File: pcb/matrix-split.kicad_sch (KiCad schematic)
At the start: 115 parts, among them J1 AudioJack4, J4 DBG, SW1 Switch, SW10 Switch, SW11 Switch, SW12 Switch, SW13 Switch, SW14 Switch, SW15 Switch, SW16 Switch, SW17 Switch, SW18 Switch, SW19 Switch, SW2 Switch, SW20 Switch, SW21 Switch, SW22 Switch, SW23 Switch, SW24 Switch, SW25 Switch, SW26 Switch, SW27 Switch, SW28 Switch, SW29 Switch, SW3 Switch, SW30 Reset_Switch, SW31 BootSel_Switch, SW4 Switch, SW5 Switch, SW6 Switch, SW7 Switch, SW8 Switch, SW9 Switch, U1 W25Q128JVS, U2 RP2040, U3 NCP1117-3.3_SOT223, Y1 Crystal_GND24

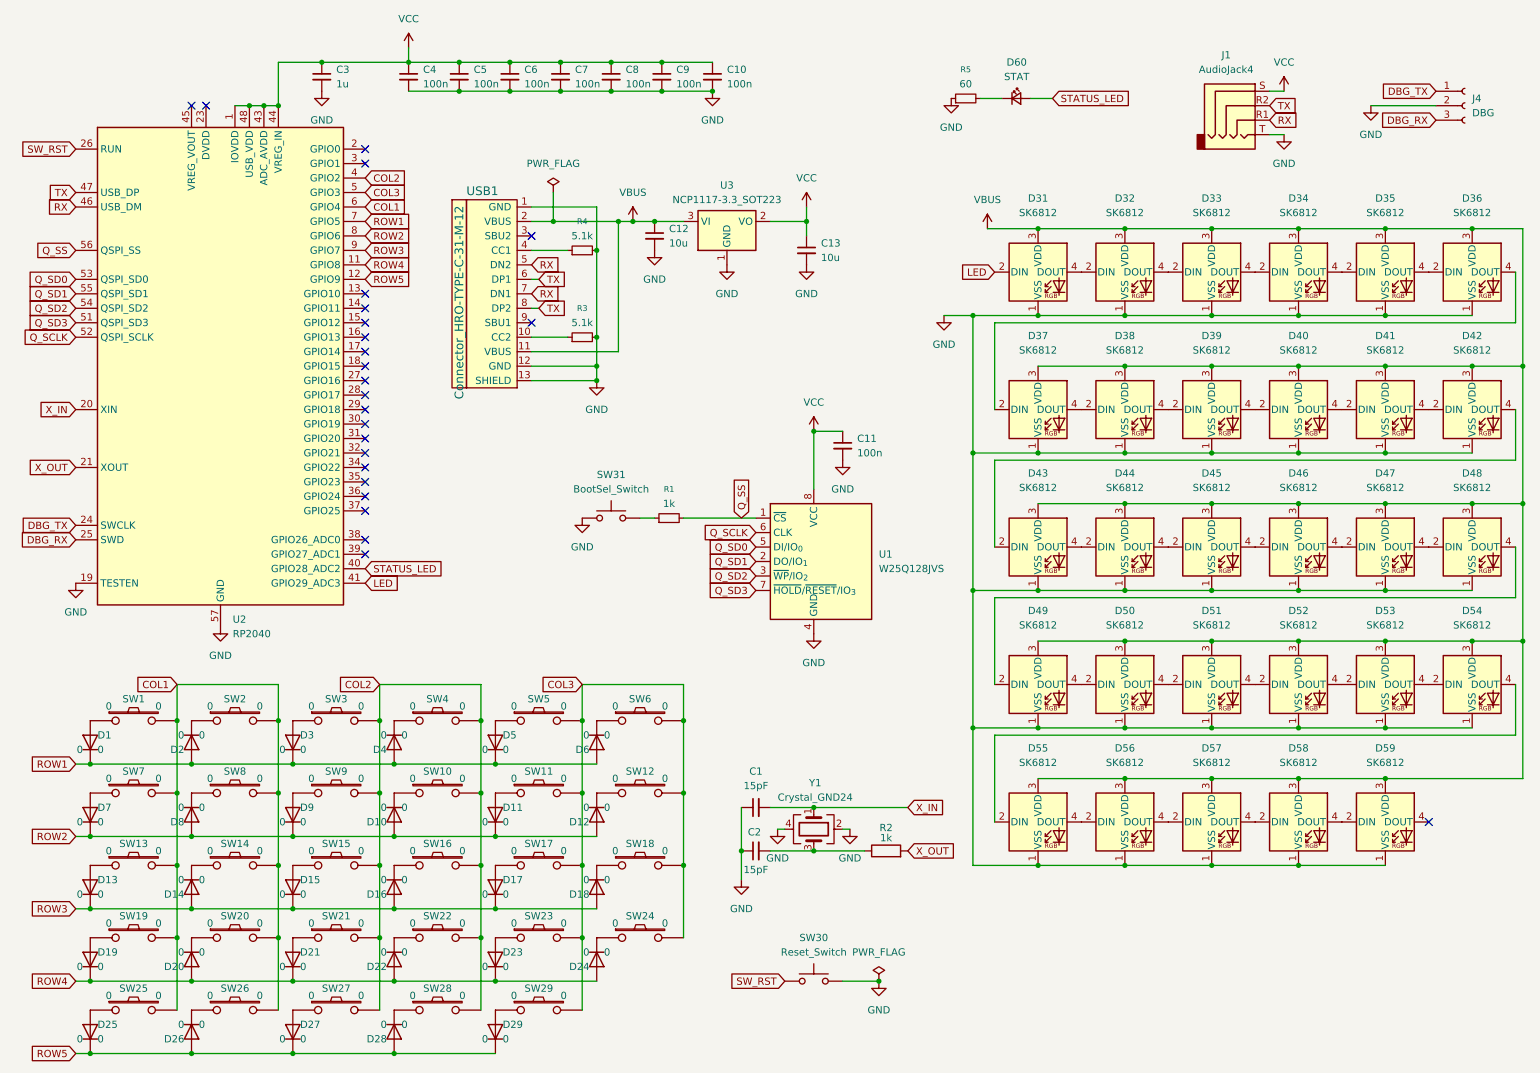
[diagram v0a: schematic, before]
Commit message: updating routing and pcb layout
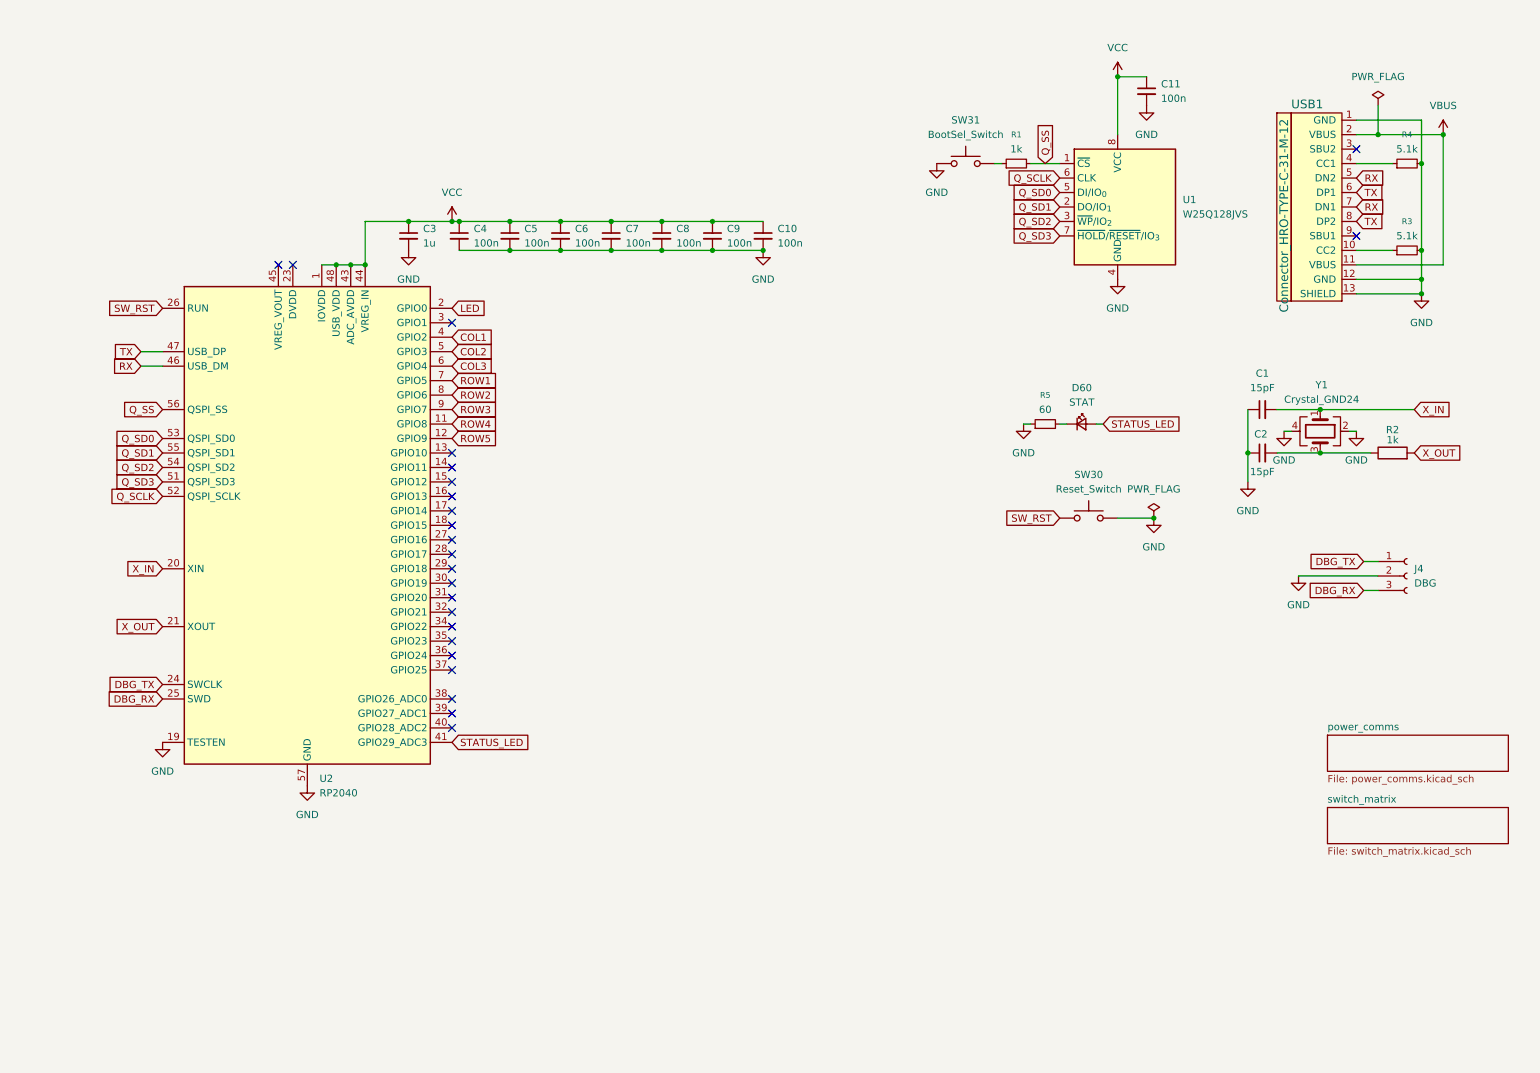
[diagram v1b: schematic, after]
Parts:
- removed C12, C13: 10u, Capacitor_SMD:C_0805_2012Metric, symbol Device:C_Small
- removed D1, D10, D11, D12, D13, D14, D15, D16, D17, D18, D19, D2, D20, D21, D22, D23, D24, D25, D26, D27, D28, D29, D3, D4, D5, D6, D7, D8, D9: Diode, Diode_SMD:D_0805_2012Metric, symbol zzkeeb:Diode
- removed D31, D32, D33, D34, D35, D36, D37, D38, D39, D40, D41, D42, D43, D44, D45, D46, D47, D48, D49, D50, D51, D52, D53, D54, D55, D56, D57, D58, D59: SK6812, LED_SMD:LED_SK6812_PLCC4_5.0x5.0mm_P3.2mm, symbol LED:SK6812
- removed J1: AudioJack4, PCM_marbastlib-xp-various:CON_MJ-4PP-9_Reversible, symbol Connector_Audio:AudioJack4
- removed SW1, SW10, SW11, SW12, SW13, SW14, SW15, SW16, SW17, SW18, SW19, SW2, SW20, SW21, SW22, SW23, SW24, SW25, SW26, SW27, SW28, SW29, SW3, SW4, SW5, SW6, SW7, SW8, SW9: Switch, keyswitches.pretty-master:Kailh_socket_PG1350, symbol zzkeeb:Switch
- removed U3: NCP1117-3.3_SOT223, Package_TO_SOT_SMD:SOT-223-3_TabPin2, symbol Regulator_Linear:NCP1117-3.3_SOT223
- USB1: footprint Type-C.pretty-master:HRO-TYPE-C-31-M-12-HandSoldering -> Type-C:HRO-TYPE-C-31-M-12-HandSoldering
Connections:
- net COL1: now also U2.4 (GPIO2); no longer U2.6 (GPIO4)
- net COL2: now also U2.5 (GPIO3); no longer U2.4 (GPIO2)
- net COL3: now also U2.6 (GPIO4); no longer U2.5 (GPIO3)
- net LED: now also U2.2 (GPIO0); no longer U2.41 (GPIO29_ADC3)
- net STATUS_LED: now also U2.41 (GPIO29_ADC3); no longer U2.40 (GPIO28_ADC2)
- no-connect marks 25 -> 24
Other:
- added sheet power_comms (power_comms.kicad_sch)
- added sheet switch_matrix (switch_matrix.kicad_sch)
- moved on the sheet: C1, C10, C11, C2, C3, C4, C5, C6, C7, C8, C9, D60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
